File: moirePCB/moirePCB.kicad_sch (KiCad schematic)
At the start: 57 parts, among them J1 USB_C_Receptacle, J2 Conn_01x06_Socket, U1 ESP32-PICO-D4, U1 TLC555xD, U10 TLV73333PDBV, U2 BQ25504, U3 TLV73333PDBV, U4 RFM95W-915S2, U5 CH340E, U7 HDC1080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

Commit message: initial pcb 3 layout
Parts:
- C3: footprint (none) -> Capacitor_SMD:C_0805_2012Metric
- C_FLTR1: renamed from C_FLTR; footprint (none) -> Capacitor_SMD:C_0805_2012Metric
- C_HVR1: renamed from C_HVR; footprint (none) -> Capacitor_SMD:C_0805_2012Metric
- C_STOR1: renamed from C_STOR; footprint (none) -> Capacitor_SMD:C_0805_2012Metric
- L_BST1: renamed from L_BST; footprint (none) -> Inductor_SMD:L_0805_2012Metric
- R_OC_1, R_OC_2, R_OK_1, R_OK_2, R_OK_3, R_OV_1, R_OV_2, R_UV_1, R_UV_2: footprint (none) -> Resistor_SMD:R_0805_2012Metric
- renumbered USB//SOLAR to USB//SOLAR1
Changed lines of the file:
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@@
       (effects (font (size 1.27 1.27)))
     )
-    (property "Footprint" "" (at 21.59 135.128 90)
+    (property "Footprint" "Resistor_SMD:R_0805_2012Metric" (at 21.59 135.128 90)
       (effects (font (size 1.27 1.27)) hide)
     )
@@
   (symbol (lib_id "Device:C") (at 81.28 172.72 270) (unit 1)
     (in_bom yes) (on_board yes) (dnp no)
-    (property "Reference" "C_STOR" (at 81.28 177.8 90)
+    (property "Reference" "C_STOR1" (at 81.28 177.8 90)
       (effects (font (size 1.27 1.27)))
     )
@@
       (effects (font (size 1.27 1.27)))
     )
-    (property "Footprint" "" (at 77.47 173.6852 0)
+    (property "Footprint" "Capacitor_SMD:C_0805_2012Metric" (at 77.47 173.6852 0)
       (effects (font (size 1.27 1.27)) hide)
     )
@@
       (project "moirePCB"
         (path "/527e949b-eaeb-4cf3-9920-57a6631a4ccb"
-          (reference "C_STOR") (unit 1)
+          (reference "C_STOR1") (unit 1)
         )
       )
@@
   (symbol (lib_id "Device:C") (at 59.69 116.84 180) (unit 1)
     (in_bom yes) (on_board yes) (dnp no) (fields_autoplaced)
-    (property "Reference" "C_HVR" (at 55.88 118.11 0)
+    (property "Reference" "C_HVR1" (at 55.88 118.11 0)
       (effects (font (size 1.27 1.27)) (justify left))
     )
@@
       (effects (font (size 1.27 1.27)) (justify left))
     )
-    (property "Footprint" "" (at 58.7248 113.03 0)
+    (property "Footprint" "Capacitor_SMD:C_0805_2012Metric" (at 58.7248 113.03 0)
       (effects (font (size 1.27 1.27)) hide)
     )
@@
       (project "moirePCB"
         (path "/527e949b-eaeb-4cf3-9920-57a6631a4ccb"
-          (reference "C_HVR") (unit 1)
+          (reference "C_HVR1") (unit 1)
         )
       )
@@
       (effects (font (size 1.27 1.27)))
     )
-    (property "Footprint" "" (at 29.21 135.128 90)
+    (property "Footprint" "Resistor_SMD:R_0805_2012Metric" (at 29.21 135.128 90)
       (effects (font (size 1.27 1.27)) hide)
     )
@@
   (symbol (lib_id "Device:C") (at 81.28 166.37 90) (unit 1)
     (in_bom yes) (on_board yes) (dnp no) (fields_autoplaced)
-    (property "Reference" "C_FLTR" (at 81.28 158.75 90)
+    (property "Reference" "C_FLTR1" (at 81.28 158.75 90)
       (effects (font (size 1.27 1.27)))
     )
@@
       (effects (font (size 1.27 1.27)))
     )
-    (property "Footprint" "" (at 85.09 165.4048 0)
+    (property "Footprint" "Capacitor_SMD:C_0805_2012Metric" (at 85.09 165.4048 0)
       (effects (font (size 1.27 1.27)) hide)
     )
@@
       (project "moirePCB"
         (path "/527e949b-eaeb-4cf3-9920-57a6631a4ccb"
-          (reference "C_FLTR") (unit 1)
+          (reference "C_FLTR1") (unit 1)
         )
       )
@@
       (effects (font (size 1.27 1.27)) (justify right))
     )
-    (property "Footprint" "" (at 50.038 133.35 90)
+    (property "Footprint" "Resistor_SMD:R_0805_2012Metric" (at 50.038 133.35 90)
       (effects (font (size 1.27 1.27)) hide)
     )
@@
   (symbol (lib_id "Switch:SW_DPDT_x2") (at 53.34 133.35 90) (unit 1)
     (in_bom yes) (on_board yes) (dnp no)
-    (property "Reference" "USB//SOLAR" (at 62.23 133.35 0)
+    (property "Reference" "USB//SOLAR1" (at 62.23 133.35 0)
       (effects (font (size 1.27 1.27)))
     )
@@
       (project "moirePCB"
         (path "/527e949b-eaeb-4cf3-9920-57a6631a4ccb"
-          (reference "USB//SOLAR") (unit 1)
+          (reference "USB//SOLAR1") (unit 1)
         )
       )
@@
   (symbol (lib_id "Device:L") (at 63.5 124.46 0) (unit 1)
     (in_bom yes) (on_board yes) (dnp no) (fields_autoplaced)
-    (property "Reference" "L_BST" (at 62.23 125.73 0)
+    (property "Reference" "L_BST1" (at 62.23 125.73 0)
       (effects (font (size 1.27 1.27)) (justify right))
     )
@@
       (effects (font (size 1.27 1.27)) (justify right))
     )
-    (property "Footprint" "" (at 63.5 124.46 0)
+    (property "Footprint" "Inductor_SMD:L_0805_2012Metric" (at 63.5 124.46 0)
       (effects (font (size 1.27 1.27)) hide)
     )
@@
       (project "moirePCB"
         (path "/527e949b-eaeb-4cf3-9920-57a6631a4ccb"
-          (reference "L_BST") (unit 1)
+          (reference "L_BST1") (unit 1)
         )
       )
@@
       (effects (font (size 1.27 1.27)))
     )
-    (property "Footprint" "" (at 12.7 164.592 90)
+    (property "Footprint" "Resistor_SMD:R_0805_2012Metric" (at 12.7 164.592 90)
       (effects (font (size 1.27 1.27)) hide)
     )
@@
       (effects (font (size 1.27 1.27)) (justify right))
     )
-    (property "Footprint" "" (at 20.828 154.94 90)
+    (property "Footprint" "Resistor_SMD:R_0805_2012Metric" (at 20.828 154.94 90)
       (effects (font (size 1.27 1.27)) hide)
     )
@@
       (effects (font (size 1.27 1.27)) (justify left))
     )
-    (property "Footprint" "" (at 17.018 138.43 90)
+    (property "Footprint" "Resistor_SMD:R_0805_2012Metric" (at 17.018 138.43 90)
       (effects (font (size 1.27 1.27)) hide)
     )
@@
       (effects (font (size 1.27 1.27)) (justify right))
     )
-    (property "Footprint" "" (at 20.828 162.56 90)
+    (property "Footprint" "Resistor_SMD:R_0805_2012Metric" (at 20.828 162.56 90)
       (effects (font (size 1.27 1.27)) hide)
     )
@@
       (effects (font (size 1.27 1.27)) (justify left))
     )
-    (property "Footprint" "" (at 17.018 146.05 90)
+    (property "Footprint" "Resistor_SMD:R_0805_2012Metric" (at 17.018 146.05 90)
       (effects (font (size 1.27 1.27)) hide)
     )
@@
       (effects (font (size 1.27 1.27)))
     )
-    (property "Footprint" "" (at 34.29 176.8348 0)
+    (property "Footprint" "Capacitor_SMD:C_0805_2012Metric" (at 34.29 176.8348 0)
       (effects (font (size 1.27 1.27)) hide)
     )
@@
       (effects (font (size 1.27 1.27)) (justify left))
     )
-    (property "Footprint" "" (at 40.132 125.73 90)
-      (effects (font (size 1.27 1.27)) hide)
-    )
+    (property "Footprint" "Resistor_SMD:R_0805_2012Metric" (at 40.132 125.73 90)
+      (effects (font (size 1.27 1.27)) hide)
+    )

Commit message: r values needed
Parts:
- added VBAT_OK: SolderJumper_2_Bridged, Jumper:SolderJumper-2_P1.3mm_Bridged_RoundedPad1.0x1.5mm, symbol Jumper:SolderJumper_2_Bridged
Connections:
- net IN: no longer BT1.1 (+), U2.14 (VBAT), U8.4 (IN), U8.6 (IN)
- net VBAT_OK: now also VBAT_OK.1 (A); no longer U10.3 (EN)
- new net: BT1.1 (+), U2.14 (VBAT), U8.4 (IN), U8.6 (IN)
- new net: U10.3 (EN), VBAT_OK.2 (B)
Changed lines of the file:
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@@
+    (stroke (width 0) (type default))
+  )
+  (wire (pts (xy 59.69 194.31) (xy 57.15 194.31))
     (stroke (width 0) (type default))
   )
@@
     (stroke (width 0) (type default))
   )
+  (wire (pts (xy 67.31 194.31) (xy 71.12 194.31))
+    (stroke (width 0) (type default))
+  )
   (wire (pts (xy 48.26 137.16) (xy 48.26 139.7))
     (stroke (width 0) (type default))
@@
   )
   (wire (pts (xy 100.33 176.53) (xy 100.33 184.15))
+    (stroke (width 0) (type default))
+  )
+  (wire (pts (xy 71.12 194.31) (xy 71.12 191.77))
     (stroke (width 0) (type default))
   )
@@
     )
   )
-  (global_label "VBAT_OK" (shape input) (at 71.12 191.77 180) (fields_autoplaced)
+  (global_label "VBAT_OK" (shape input) (at 57.15 194.31 180) (fields_autoplaced)
     (effects (font (size 1.27 1.27)) (justify right))
-    (property "Intersheetrefs" "${INTERSHEET_REFS}" (at 60.1519 191.77 0)
+    (property "Intersheetrefs" "${INTERSHEET_REFS}" (at 46.1819 194.31 0)
       (effects (font (size 1.27 1.27)) (justify right) hide)
     )
@@
     )
   )
-  (symbol (lib_id "Power_Management:AP2281-1WG-7") (at 114.3 167.64 0) (unit 1)
+  (symbol (lib_name "AP2281-1WG-7_1") (lib_id "Power_Management:AP2281-1WG-7") (at 114.3 167.64 0) (unit 1)
     (in_bom yes) (on_board yes) (dnp no) (fields_autoplaced)
     (property "Reference" "U8" (at 114.3 158.75 0)
@@
       (effects (font (size 1.27 1.27)) hide)
     )
-    (property "Datasheet" "https://www.diodes.com/assets/Datasheets/AP2161.pdf" (at 114.3 166.37 0)
+    (property "Datasheet" "https://www.diodes.com/assets/Datasheets/AP2161.pdf" (at 114.3 160.02 0)
       (effects (font (size 1.27 1.27)) hide)
     )
@@
         )
       )
+    )
+  )
+  (symbol (lib_id "Jumper:SolderJumper_2_Bridged") (at 63.5 194.31 0) (unit 1)
+    (in_bom yes) (on_board yes) (dnp no)
+    (property "Reference" "VBAT_OK" (at 59.69 196.85 0)
+      (effects (font (size 1.27 1.27)) (justify left))
+    )
+    (property "Value" "SolderJumper_2_Bridged" (at 68.58 196.85 0)
+      (effects (font (size 1.27 1.27)) (justify left) hide)
+    )
+    (property "Footprint" "Jumper:SolderJumper-2_P1.3mm_Bridged_RoundedPad1.0x1.5mm" (at 63.5 194.31 0)
+      (effects (font (size 1.27 1.27)) hide)
+    )
+    (property "Datasheet" "~" (at 63.5 194.31 0)
+      (effects (font (size 1.27 1.27)) hide)
+    )
+    (pin "1")
+    (pin "2")
+    (instances
+      (project "moirePCB"
+        (path "/527e949b-eaeb-4cf3-9920-57a6631a4ccb"
+          (reference "VBAT_OK") (unit 1)
+        )
+      )

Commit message: pre route
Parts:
- BT1: footprint Battery:BatteryHolder_Keystone_1060_1x2032 -> Connector_JST:JST_EH_S2B-EH_1x02_P2.50mm_Horizontal
- SC1: footprint (none) -> Connector_PinHeader_2.54mm:PinHeader_1x02_P2.54mm_Horizontal
- renumbered VBAT_OK to VBAT_OK1
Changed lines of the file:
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@@
       (effects (font (size 1.27 1.27)) (justify left))
     )
-    (property "Footprint" "Battery:BatteryHolder_Keystone_1060_1x2032" (at 100.33 172.466 90)
+    (property "Footprint" "Connector_JST:JST_EH_S2B-EH_1x02_P2.50mm_Horizontal" (at 100.33 172.466 90)
       (effects (font (size 1.27 1.27)) hide)
     )
@@
   (symbol (lib_id "Jumper:SolderJumper_2_Bridged") (at 63.5 194.31 0) (unit 1)
     (in_bom yes) (on_board yes) (dnp no)
-    (property "Reference" "VBAT_OK" (at 59.69 196.85 0)
+    (property "Reference" "VBAT_OK1" (at 59.69 196.85 0)
       (effects (font (size 1.27 1.27)) (justify left))
     )
@@
       (project "moirePCB"
         (path "/527e949b-eaeb-4cf3-9920-57a6631a4ccb"
-          (reference "VBAT_OK") (unit 1)
+          (reference "VBAT_OK1") (unit 1)
         )
       )
@@
       (effects (font (size 1.27 1.27)) (justify left))
     )
-    (property "Footprint" "" (at 67.31 117.094 90)
-      (effects (font (size 1.27 1.27)) hide)
-    )
+    (property "Footprint" "Connector_PinHeader_2.54mm:PinHeader_1x02_P2.54mm_Horizontal" (at 67.31 117.094 90)
+      (effects (font (size 1.27 1.27)) hide)
+    )

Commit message: resistorValues
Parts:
- added R_OC+10: 10M, Resistor_SMD:R_0805_2012Metric, symbol Device:R
- R_OC_1: value R -> 5.76M
- R_OC_2: value R -> 4.12M
- R_OK_1: value R -> 3.57M
- R_OK_2, R_UV_2: value R -> 6.19M
- R_OK_3: value R -> .143M
- R_OV_1: value R -> 4.42M
- R_OV_2: value R -> 5.36M
- R_UV_1: value R -> 3.74M
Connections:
- net at R_OC_2.1, U2.2 (VIN_DC), USB//SOLAR1.2 (B): now also L_BST1.1
- net at R_OC_1.2, U2.3 (VOC_SAMP): now also R_OC+10.2; no longer R_OC_2.2
- net at C_HVR1.1, SC1.1 (+), USB//SOLAR1.3 (C): no longer L_BST1.1
- new net: R_OC+10.1, R_OC_2.2
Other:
- note removed: "check this"
- moved on the sheet: L_BST1, R_OC_1, R_OC_2, USB//SOLAR1A

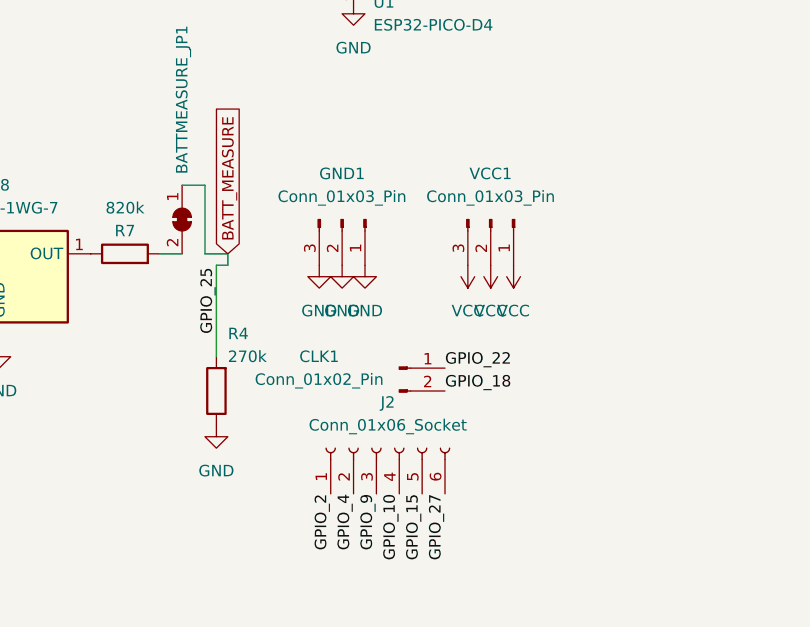
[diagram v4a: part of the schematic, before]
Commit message: hole battery outline
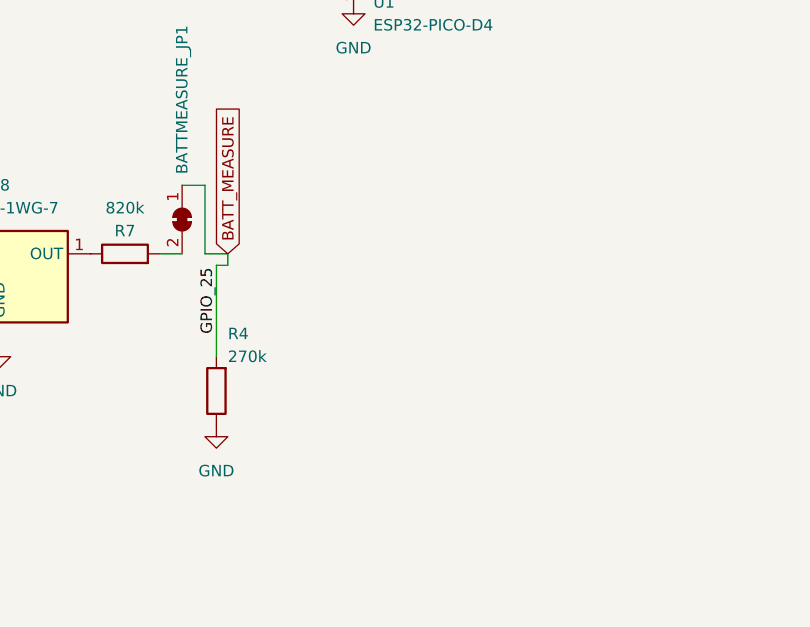
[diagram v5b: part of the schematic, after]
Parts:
- removed CLK1: Conn_01x02_Pin, Connector_PinSocket_2.54mm:PinSocket_1x02_P2.54mm_Vertical, symbol Connector:Conn_01x02_Pin
- removed GND1, VCC1: Conn_01x03_Pin, Connector_PinSocket_2.54mm:PinSocket_1x03_P2.54mm_Vertical, symbol Connector:Conn_01x03_Pin
- removed J2: Conn_01x06_Socket, Connector_PinSocket_2.54mm:PinSocket_1x06_P2.54mm_Vertical, symbol Connector:Conn_01x06_Socket

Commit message: pcb3 prod
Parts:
- BT1: footprint Connector_JST:JST_EH_S2B-EH_1x02_P2.50mm_Horizontal -> Connector_JST:JST_PH_S2B-PH-K_1x02_P2.00mm_Horizontal; LCSC (none) -> C173752
- L_BST1: LCSC (none) -> C6364733
- R_OC_2: LCSC (none) -> C422734
- U1: LCSC (none) -> C6987
- U4: LCSC (none) -> C2844472
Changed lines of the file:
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@@
       (effects (font (size 1.27 1.27)) (justify left))
     )
-    (property "Footprint" "Connector_JST:JST_EH_S2B-EH_1x02_P2.50mm_Horizontal" (at 100.33 172.466 90)
+    (property "Footprint" "Connector_JST:JST_PH_S2B-PH-K_1x02_P2.00mm_Horizontal" (at 100.33 172.466 90)
       (effects (font (size 1.27 1.27)) hide)
     )
     (property "Datasheet" "~" (at 100.33 172.466 90)
+      (effects (font (size 1.27 1.27)) hide)
+    )
+    (property "LCSC" "C173752" (at 100.33 173.99 0)
       (effects (font (size 1.27 1.27)) hide)
     )
@@
       (effects (font (size 1.27 1.27)) hide)
     )
+    (property "LCSC" "C422734" (at 48.26 135.89 0)
+      (effects (font (size 1.27 1.27)) hide)
+    )
     (pin "1")
     (pin "2")
@@
     )
     (property "Datasheet" "http://www.ti.com/lit/ds/symlink/tlc555.pdf" (at 68.58 90.17 0)
+      (effects (font (size 1.27 1.27)) hide)
+    )
+    (property "LCSC" "C6987" (at 46.99 80.01 0)
       (effects (font (size 1.27 1.27)) hide)
     )
@@
       (effects (font (size 1.27 1.27)) hide)
     )
+    (property "LCSC" "C6364733" (at 63.5 137.16 0)
+      (effects (font (size 1.27 1.27)) hide)
+    )
     (pin "1")
     (pin "2")
@@
       (effects (font (size 1.27 1.27)))
     )
-    (pin "1")
+    (property "LCSC" "C2844472" (at 254 39.37 0)
+      (effects (font (size 1.27 1.27)) hide)
+    )
+    (pin "1")
